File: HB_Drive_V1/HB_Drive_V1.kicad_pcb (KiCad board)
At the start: 2 copper layers, 253.2 x 77 mm, 271 parts, among them J1002 Conn_02x04_Odd_Even, J201 Conn_02x02_Odd_Even, J202 Conn_02x03_Odd_Even, J203 Conn_01x03, J301 Conn_02x03_Odd_Even, J303 Conn_01x02, J304 Conn_02x04_Odd_Even, J401 Conn_01x03, J501 54-00164, J502 5227699-1, J503 USB-B-S-X-X-VT, J505 Conn_01x03, J506 3M_30306-6002HB, J701 Conn_02x02_Odd_Even, J702 Conn_02x02_Odd_Even, J801 Conn_02x03_Odd_Even, SW701 SW_PTS636S-J_CNK, SW704 SW_PTS636S-J_CNK, U1001 NE555D, U1003 TL082, U1004 TL082, U201 TL082, U202 TL082, U203 TL082, U204 TL082, U205 TL082, U301 TL082, U302 TL082, U303 TL082, U304 TL082, U305 TL082, U401 LM311, U402 74LS08, U403 74AHC1G125, U404 74AHC1GU04, U405 74AHC1GU04, U406 74AHC1G125, U501 REF102CU, U502 R-78E5.0-0.5, U503 TL082, U504 TL082, U505 TMH 0515D, U506 AMS1117-3.3, U702 74LS32, U703 TL082, U704 TL082, U705 LM311, U706 74LS02

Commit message: Preliminary wiring of V2, Passes DRC, awaiting review
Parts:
- moved R211 1.54 mm to (290.4, 199.0)
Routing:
- net GND: track 34.2 -> 29.2 mm, vias 479 -> 477
- net -15V: track 726.7 -> 722.9 mm
- net /Inner Current Regulator/+I_Err: track 107.6 -> 103.8 mm
- net +9V: track 85.1 -> 88.7 mm
- net +5V: track 638.1 -> 640.5 mm
- net +15V: track 867.9 -> 869.3 mm
- net Net-(U205B--): track 0.00 -> 1.27 mm
- net /Modulator and Protection/Protection/Overcurrent: track 48.2 -> 47.1 mm
- net /Modulator and Protection/Protection/I_Abs: track 30.2 -> 29.2 mm, vias 1 -> 0
- net Net-(U204B--): track 20.7 -> 19.9 mm
- net /Int_Cmd: track 140.8 -> 141.5 mm
- net Net-(R211-Pad2): track 8.76 -> 9.28 mm
- net /Inner Current Regulator/-I_Fdbk: track 144.5 -> 145.0 mm
- net /Ext_Cmd: vias 3 -> 2
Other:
- board text added: "+I_Cmd"
- board text added: "-I_Cmd"
- board text added: "Frequency Select"
- board text added: "HB DRIVE V2"
- board text added: "H_Raw"
- board text added: "Inner EN"
- board text added: "Outer EN"
- board text added: "V_Fdbk1, V_Fdbk2"
- board text removed: "HB DRIVE V1"

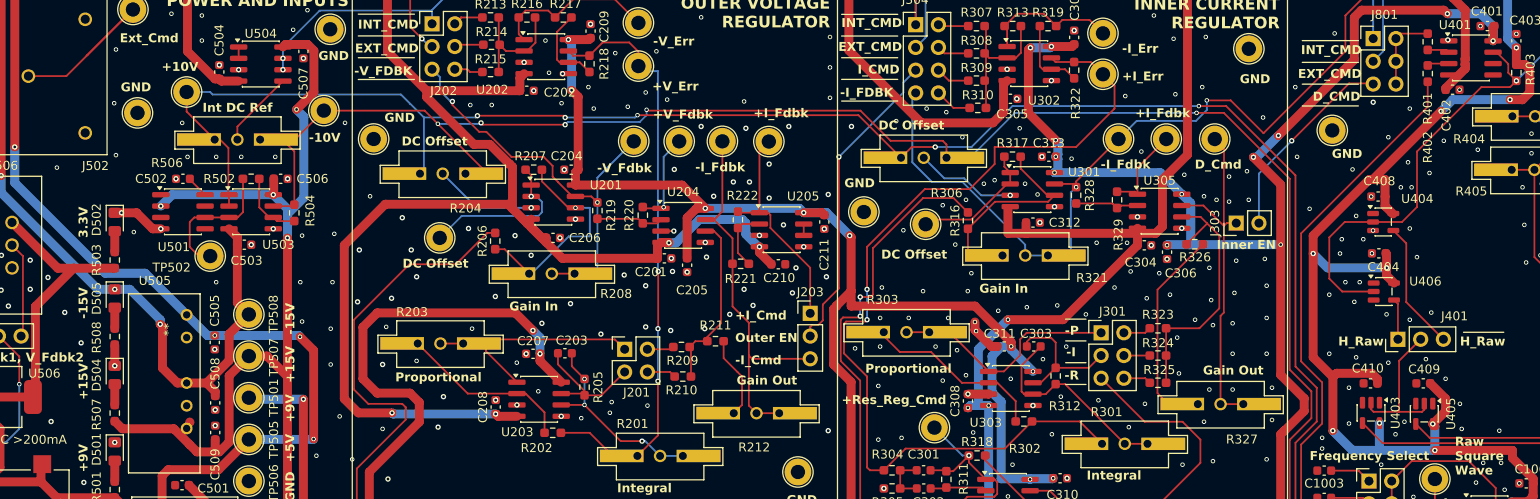
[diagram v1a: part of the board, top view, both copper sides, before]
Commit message: Updates to 1st review corrected V2 of board
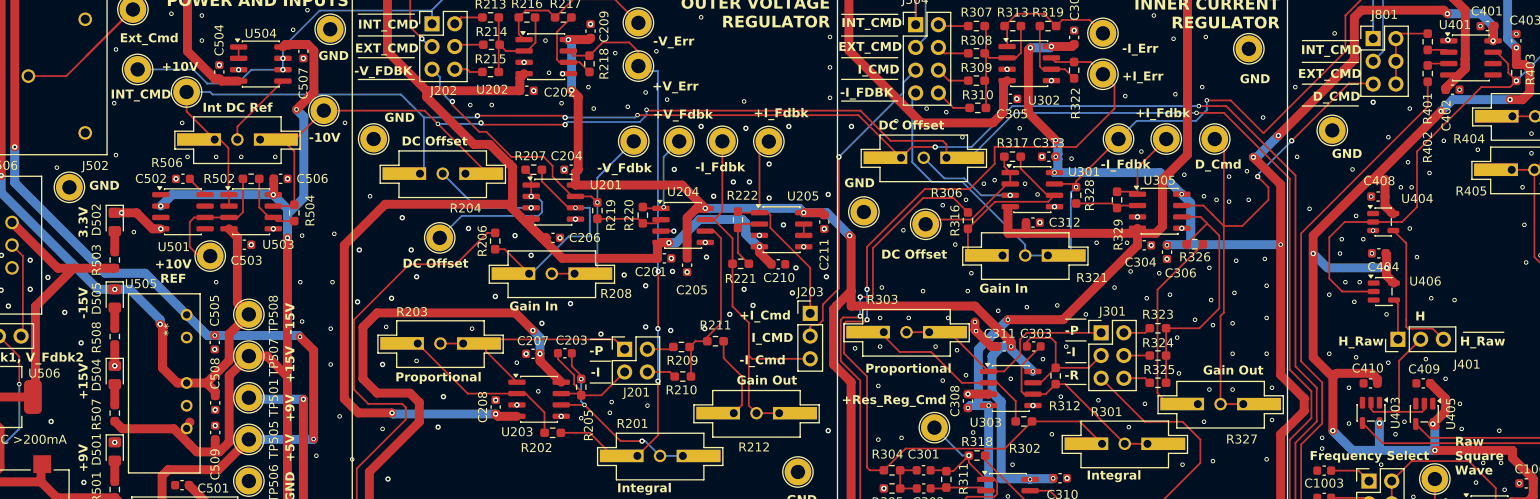
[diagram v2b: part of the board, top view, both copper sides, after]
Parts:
- removed J303: Conn_01x02, Connector_PinHeader_2.54mm:PinHeader_1x02_P2.54mm_Vertical
- added TP522: TestPoint, TestPoint:TestPoint_Loop_D2.60mm_Drill1.6mm_Beaded, F.Cu at (225.8, 168.6)
- C1002: value 100pF 50V -> 200pF 50V
- C1003: value 100pF 50V -> 400pF 50V
- J506: value 3M_30306-6002HB -> 30306-6002HB
- SW701, SW704: value SW_PTS636S-J_CNK -> PTS636SL43SMTRLFS
- moved TP512 11.3 mm to (218.2, 181.8)
- moved R205 0.37 mm to (275.4, 204.1)
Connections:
- R327 pad 2: Net-(J303-Pin_1) -> /Inner Current Regulator/D_Cmd
- R327 pad 3: Net-(J303-Pin_1) -> /Inner Current Regulator/D_Cmd
- TP306 pad 1: Net-(J303-Pin_1) -> /Inner Current Regulator/D_Cmd
- U305 pad 7: Net-(J303-Pin_1) -> /Inner Current Regulator/D_Cmd
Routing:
- net /Inner Current Regulator/D_Cmd: track 22.4 -> 65.3 mm, vias 1 -> 2
- net Net-(J303-Pin_1): track 40.3 -> 0.00 mm
- net /Int_Cmd: track 141.5 -> 159.1 mm
- net Net-(J401-Pin_3): track 14.5 -> 16.1 mm
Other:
- board text added: "+10V REF"
- board text removed: "Inner EN"
- board text removed: "Outer EN"

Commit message: restores v2 to condtion as ordered!
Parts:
- C1003: value 400pF 50V -> 470pF 50V
- R1010: value 1MΩ 5% -> 5MΩ 5%
- U501: value REF102CU -> REF102AU
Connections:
- net /Modulator and Protection/Modulator and Dead Time Injector/D_Cmd renamed /Modulator and Protection/Modulator and Dead Time Injector/Duty
- J203 pad 1: /Outer Voltage Regulator/+I_Cmd -> /Outer Voltage Regulator/-I_Cmd
- J203 pad 3: /Outer Voltage Regulator/-I_Cmd -> /Outer Voltage Regulator/+I_Cmd
- R212 pad 2: /Outer Voltage Regulator/-I_Cmd -> /Outer Voltage Regulator/+I_Cmd
- R212 pad 3: /Outer Voltage Regulator/-I_Cmd -> /Outer Voltage Regulator/+I_Cmd
- R221 pad 2: /Outer Voltage Regulator/-I_Cmd -> /Outer Voltage Regulator/+I_Cmd
- R222 pad 1: /Outer Voltage Regulator/+I_Cmd -> /Outer Voltage Regulator/-I_Cmd
- TP202 pad 1: /Outer Voltage Regulator/-I_Cmd -> /Outer Voltage Regulator/+I_Cmd
- TP206 pad 1: /Outer Voltage Regulator/+I_Cmd -> /Outer Voltage Regulator/-I_Cmd
- U204 pad 7: /Outer Voltage Regulator/-I_Cmd -> /Outer Voltage Regulator/+I_Cmd
- U205 pad 1: /Outer Voltage Regulator/+I_Cmd -> /Outer Voltage Regulator/-I_Cmd
- U403 pad 1: unconnected-(U403-Pad1) -> GND
- U406 pad 1: unconnected-(U406-Pad1) -> GND
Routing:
- net /Outer Voltage Regulator/-I_Cmd: track 44.7 -> 25.0 mm
- net /Outer Voltage Regulator/+I_Cmd: track 25.0 -> 44.7 mm
- net GND: vias 477 -> 479

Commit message: Moves Ports and adds level shifter
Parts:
- added Q701: BSS138, Package_TO_SOT_SMD:SOT-23, F.Cu at (438.4, 177.0)
- added Q702: BSS138, Package_TO_SOT_SMD:SOT-23, F.Cu at (444.2, 177.1)
- added R716: 10kΩ 1%, Resistor_SMD:R_0603_1608Metric_Pad0.98x0.95mm_HandSolder, F.Cu at (435.5, 177.0)
- added R717: 10kΩ 1%, Resistor_SMD:R_0603_1608Metric_Pad0.98x0.95mm_HandSolder, F.Cu at (434.9, 170.5)
- added R718: 10kΩ 1%, Resistor_SMD:R_0603_1608Metric_Pad0.98x0.95mm_HandSolder, F.Cu at (441.5, 177.0)
- added R719: 10kΩ 1%, Resistor_SMD:R_0603_1608Metric_Pad0.98x0.95mm_HandSolder, F.Cu at (435.0, 166.2)
- moved J506 240.7 mm to (450.0, 184.4)
- moved C511 234.6 mm to (439.0, 179.8), turned to 180 degrees
- moved J505 230.4 mm to (438.0, 190.0)
- moved U506 230.4 mm to (440.4, 184.5)
- moved C510 229.2 mm to (433.0, 178.5), turned to 0 degrees
- moved TP705 21.4 mm to (449.8, 222.0)
- moved TP706 20.0 mm to (450.0, 214.2)
- moved C702 19.3 mm to (449.9, 205.4)
- moved C711 19.3 mm to (438.7, 214.8)
- moved D704 19.3 mm to (443.9, 196.8)
- moved R711 19.3 mm to (439.4, 208.8)
- moved R712 19.3 mm to (447.0, 214.2)
- moved R714 19.3 mm to (443.6, 198.8)
- moved SW704 19.3 mm to (444.5, 218.6)
- moved U706 19.3 mm to (445.2, 207.0)
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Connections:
- C510 pad 1: +9V -> +5V
- J506 pad 2: +3.3V -> GND
- U402 pad 11: /G_Lower_Cmd -> /Modulator and Protection/Protection/G_Lower_Cmd_5V_Out
- U402 pad 8: /G_Upper_Cmd -> /Modulator and Protection/Protection/G_Upper_Cmd_5V_Out
- U506 pad 3: +9V -> +5V
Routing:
- net +3.3V: track 38.7 -> 317.0 mm, vias 0 -> 4
- net /V_Fdbk_Raw: track 140.1 -> 313.2 mm
- net /Modulator and Protection/Protection/G_Upper_Cmd_5V_Out: track 0.00 -> 58.9 mm, vias 0 -> 4
- net /I_Fdbk_Raw: track 200.8 -> 245.5 mm, vias 3 -> 4
- net /Modulator and Protection/Protection/G_Lower_Cmd_5V_Out: track 0.00 -> 41.9 mm, vias 0 -> 4
- net Net-(R711-Pad1): track 30.9 -> 45.8 mm
- net /G_Lower_Cmd: track 38.2 -> 23.5 mm, vias 2 -> 0
- net /Modulator and Protection/Protection/Protection_Latch: track 68.6 -> 82.9 mm
- net +9V: track 88.7 -> 78.3 mm
- net /G_Upper_Cmd: track 49.2 -> 39.0 mm, vias 2 -> 0
- net GND: track 29.2 -> 20.8 mm, vias 479 -> 484
- net /Connectors, Auxillaries, and References/V_Fdbk1: track 10.8 -> 13.3 mm
- net +5V: track 640.5 -> 638.8 mm, vias 24 -> 26
- net +15V: track 869.3 -> 868.0 mm, vias 35 -> 37
- net /+10V_Ref: track 312.0 -> 311.9 mm, vias 9 -> 10
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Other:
- outline, holes or cut-outs redrawn
- board text added: "Hb DrIVE V3"
- board text added: "V_Fdbk: 1,2"
- board text removed: "HB DRIVE V2"
- board text removed: "V_Fdbk1, V_Fdbk2"
